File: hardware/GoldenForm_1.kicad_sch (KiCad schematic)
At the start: 56 parts, among them IC1 UVLO, J1 1140084168, J2 Conn_01x02_Pin, J3 USB4105-GF-A, J4 Conn_01x04_Pin, J5 Conn_01x02_Pin, M1 MountingHole x 4, U1 ESP32-S3-WROOM-1, U2 BNO055, U3 Buck_Boost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

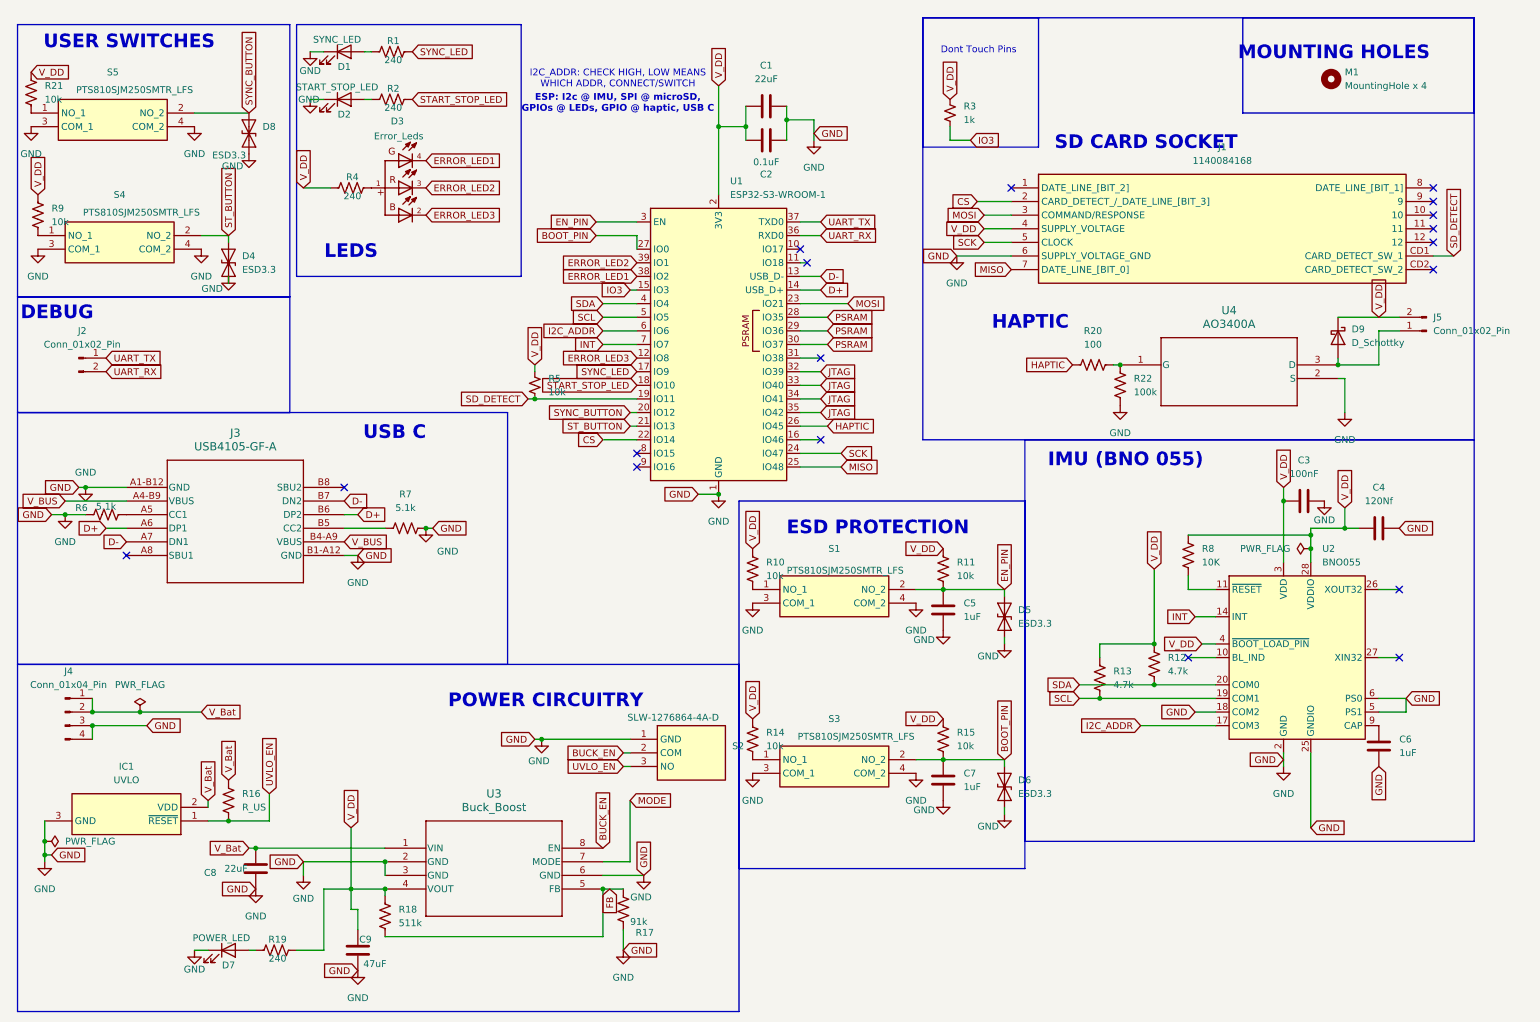
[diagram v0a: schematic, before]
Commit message: added caps for vdd sd, added esd for usbc, fixed i2c addr from bno
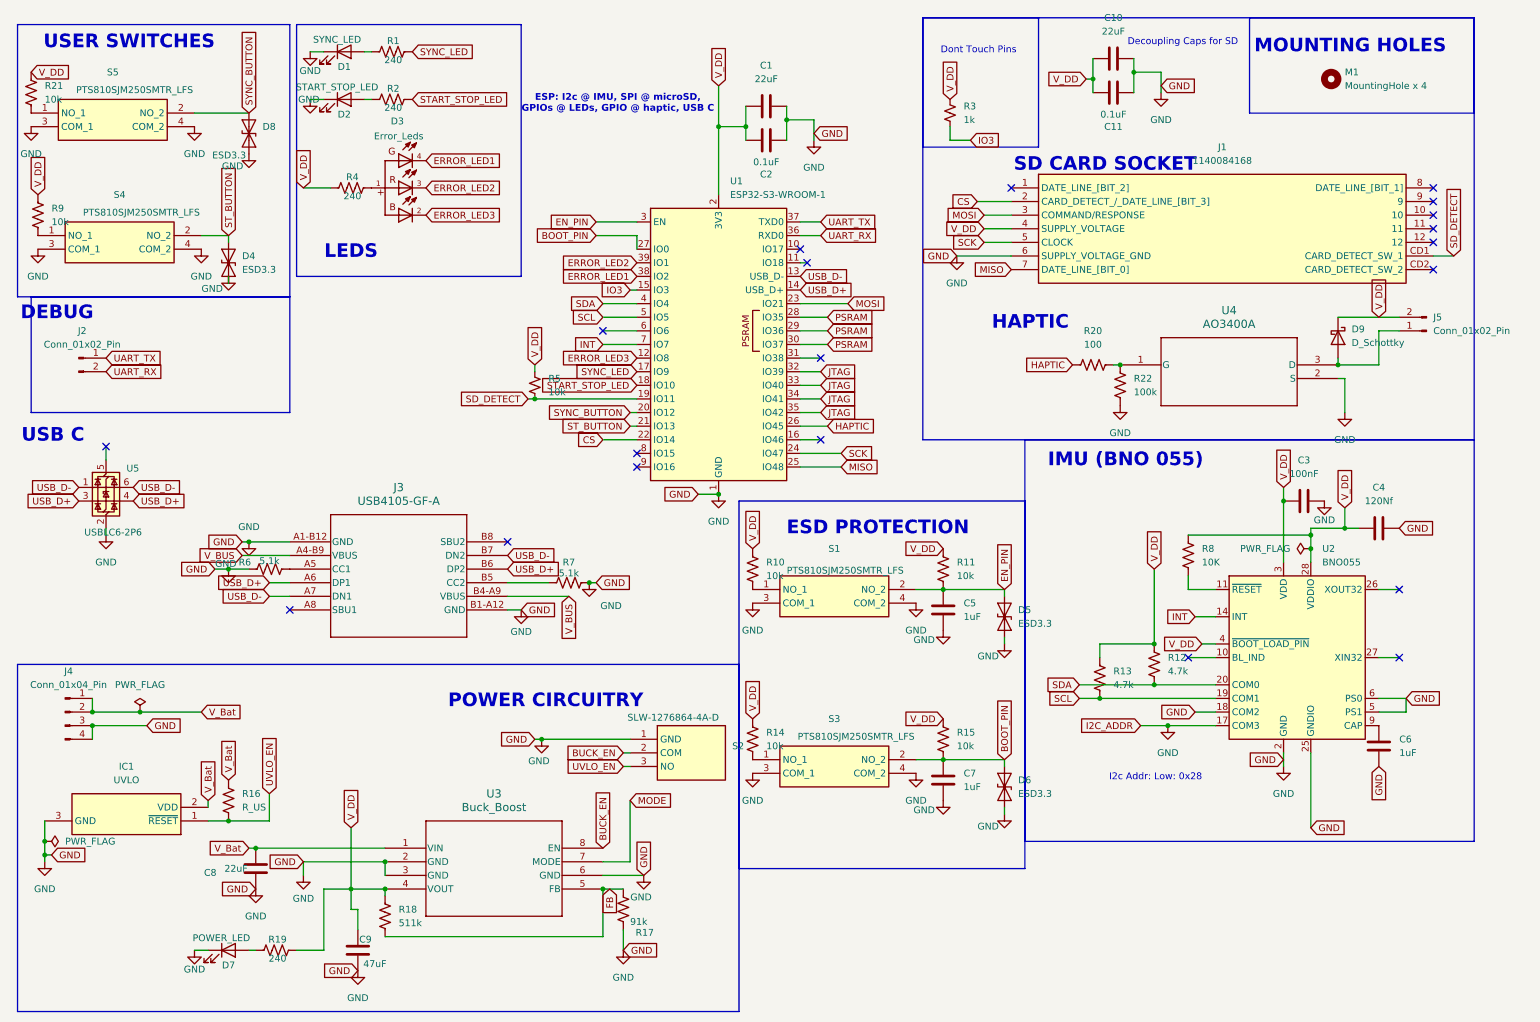
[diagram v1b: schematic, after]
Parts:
- added C10: 22uF, Capacitor_SMD:C_0805_2012Metric_Pad1.18x1.45mm_HandSolder, symbol Device:C
- added C11: 0.1uF, Capacitor_SMD:C_0805_2012Metric_Pad1.18x1.45mm_HandSolder, symbol Device:C
- added U5: USBLC6-2P6, Package_TO_SOT_SMD:SOT-666, symbol Power_Protection:USBLC6-2P6
- D4, D5, D6, D8: footprint Diode_SMD:D_SOD-923 -> Diode_SMD:D_0805_2012Metric_Pad1.15x1.40mm_HandSolder
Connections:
- net GND: now also U2.17 (COM3), C10.2, C11.2, U5.2 (GND)
- net V_DD: now also C10.1, C11.1
- net D+ renamed USB_D+
- net USB_D+: now also U5.3 (I/O2), U5.4 (I/O2)
- net D- renamed USB_D-
- net USB_D-: now also U5.1 (I/O1), U5.6 (I/O1)
- net I2C_ADDR: no longer names the net of U1.6 (IO6)
- net I2C_ADDR: no longer U2.17 (COM3)
- no-connect marks 18 -> 20
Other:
- note added: "Decoupling Caps for SD"
- note added: "I2c Addr: Low: 0x28"
- note removed: "I2C_ADDR: CHECK HIGH, LOW MEANS WHICH ADDR, CONNECT/SWITCH"
- moved on the sheet: J3, R6, R7

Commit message: 0 DRC errors. Need to do silkscreen
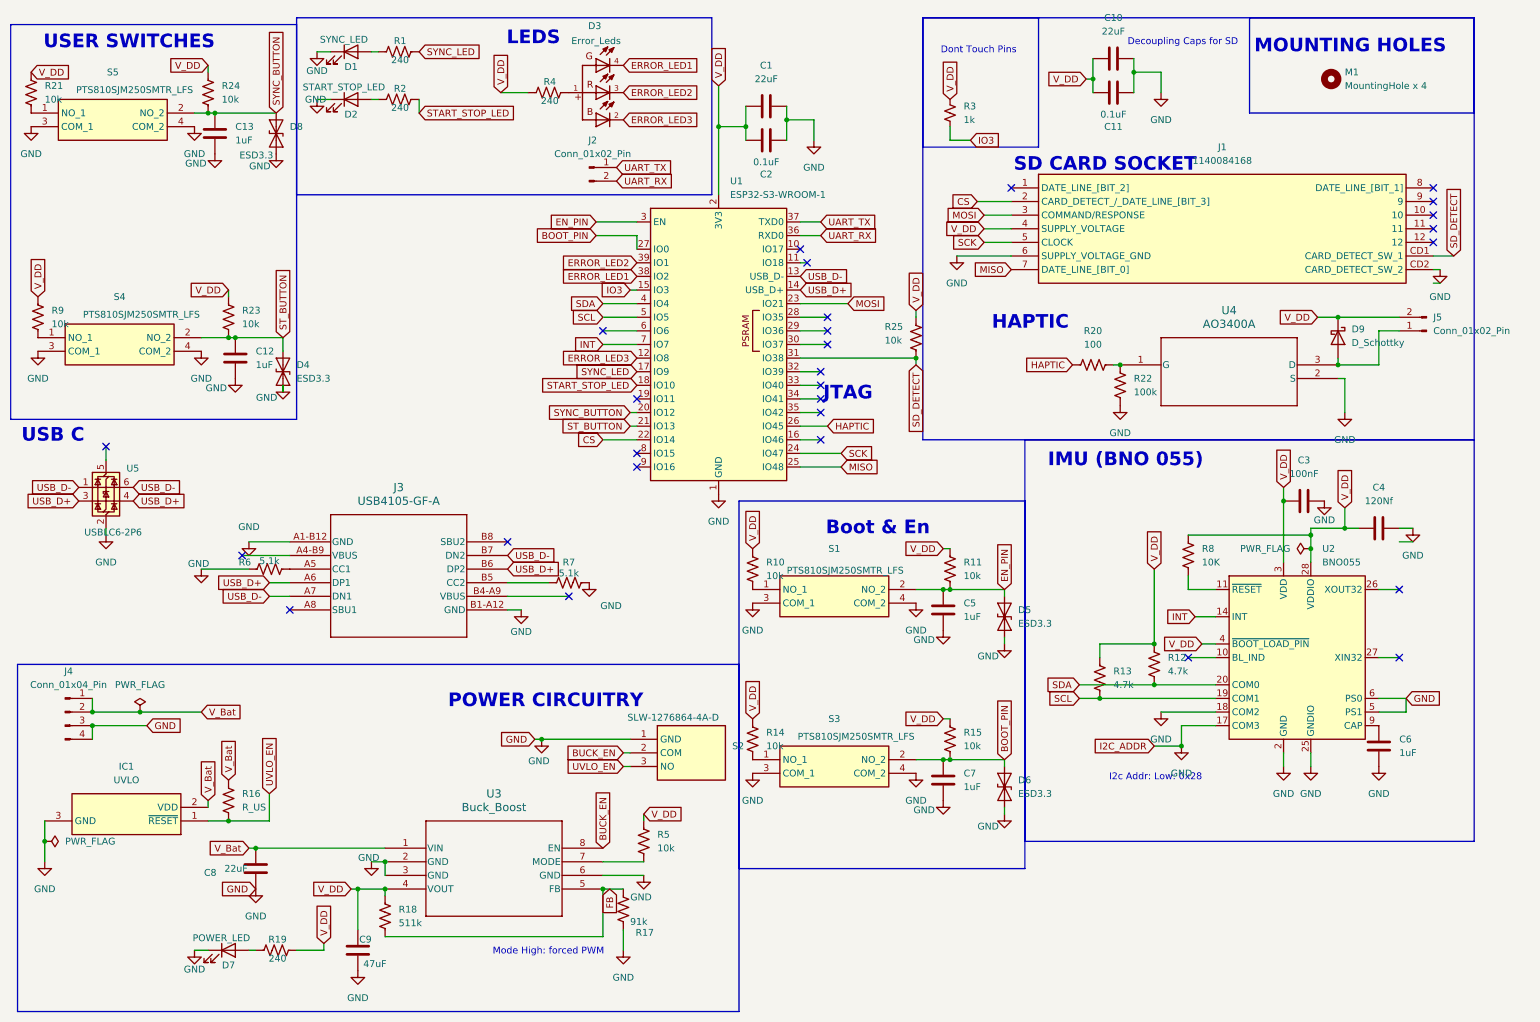
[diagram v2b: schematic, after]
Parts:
- removed R5: 10k, Resistor_SMD:R_0805_2012Metric_Pad1.20x1.40mm_HandSolder, symbol Device:R_Small_US
- added C12, C13: 1uF, Capacitor_SMD:C_0805_2012Metric_Pad1.18x1.45mm_HandSolder, symbol Device:C
- added R23, R24, R25, R5: 10k, Resistor_SMD:R_0805_2012Metric_Pad1.20x1.40mm_HandSolder, symbol Device:R_US
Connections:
- net GND: now also J1.CD2 (CARD_DETECT_SW_2), C12.2, C13.2
- net SD_DETECT: now also U1.31 (IO38), R25.2; no longer U1.19 (IO11)
- net ST_BUTTON: now also C12.1, R23.2
- net SYNC_BUTTON: now also C13.1, R24.2
- net V_DD: now also R23.1, R24.1, R25.1, R5.1
- removed net JTAG: U1.32 (IO39), U1.33 (IO40), U1.34 (IO41), U1.35 (IO42)
- net MODE: no longer names the net of U3.7 (MODE)
- net MODE: now also R5.2
- removed net PSRAM: U1.28 (IO35), U1.29 (IO36), U1.30 (IO37)
- net V_BUS: no longer names the net of J3.A4-B9 (VBUS)
- net V_BUS: no longer J3.B4-A9 (VBUS)
- no-connect marks 20 -> 28
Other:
- note added: "Boot & En"
- note added: "JTAG"
- note added: "Mode High: forced PWM"
- note removed: "DEBUG"
- note removed: "ESD PROTECTION"
- note removed: "ESP: I2c @ IMU, SPI @ microSD, GPIOs @ LEDs, GPIO @ haptic, USB C"
- moved on the sheet: D1, D2, D3, D4, D8, J2, R1, R11, R15, R2, R4, R9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

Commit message: CDR updates
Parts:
- J2: footprint Connector_PinHeader_1.00mm:PinHeader_1x02_P1.00mm_Vertical -> Connector_PinHeader_2.54mm:PinHeader_1x02_P2.54mm_Vertical
- J3: footprint USB4105_GCT -> MyFootprints:USB4105_GCT
- J4: footprint Connector_PinHeader_1.00mm:PinHeader_1x04_P1.00mm_Vertical -> Connector_PinHeader_2.54mm:PinHeader_1x04_P2.54mm_Vertical
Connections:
- net V_BUS: now reaches J3.B4-A9 (VBUS)
- net V_BUS: now also U5.5 (VBUS)
- no-connect marks 28 -> 26
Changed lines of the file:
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@@
 	)
 	(no_connect
-		(at 115.57 119.38)
-	)
-	(no_connect
 		(at 270.51 130.81)
 	)
@@
 	)
 	(no_connect
-		(at 54.61 111.76)
-	)
-	(no_connect
 		(at 163.83 69.85)
 	)
@@
 	)
 	(no_connect
-		(at 29.21 91.44)
-	)
-	(no_connect
 		(at 163.83 67.31)
 	)
@@
 	)
 	(no_connect
+		(at 54.61 111.76)
+	)
+	(no_connect
 		(at 63.5 121.92)
 	)
@@
 	(wire
 		(pts
+			(xy 104.14 119.38) (xy 106.68 119.38)
+		)
+		(stroke
+			(width 0)
+			(type default)
+		)
+	)
+	(wire
+		(pts
 			(xy 45.72 29.21) (xy 48.26 29.21)
 		)
@@
 	(wire
 		(pts
-			(xy 104.14 119.38) (xy 115.57 119.38)
-		)
-		(stroke
-			(width 0)
-			(type default)
-		)
-	)
-	(wire
-		(pts
 			(xy 180.34 149.86) (xy 185.42 149.86)
 		)
@@
 	(wire
 		(pts
+			(xy 29.21 91.44) (xy 31.75 91.44)
+		)
+		(stroke
+			(width 0)
+			(type default)
+		)
+	)
+	(wire
+		(pts
 			(xy 158.75 52.07) (xy 162.56 52.07)
 		)
@@
 		)
 	)
+	(global_label "V_BUS"
+		(shape input)
+		(at 31.75 91.44 0)
+		(fields_autoplaced yes)
+		(effects
+			(font
+				(size 1.27 1.27)
+			)
+			(justify left)
+		)
+		(property "Intersheetrefs" "${INTERSHEET_REFS}"
+			(at 40.6014 91.44 0)
+			(effects
+				(font
+					(size 1.27 1.27)
+				)
+				(justify left)
+				(hide yes)
+			)
+		)
+	)
 	(global_label "HAPTIC"
 		(shape input)
@@
 		)
 	)
+	(global_label "V_BUS"
+		(shape input)
+		(at 106.68 119.38 0)
+		(fields_autoplaced yes)
+		(effects
+			(font
+				(size 1.27 1.27)
+			)
+			(justify left)
+		)
+		(property "Intersheetrefs" "${INTERSHEET_REFS}"
+			(at 115.5314 119.38 0)
+			(effects
+				(font
+					(size 1.27 1.27)
+				)
+				(justify left)
+				(hide yes)
+			)
+		)
+	)
 	(global_label "GND"
 		(shape input)
@@
 			)
 		)
-		(property "Footprint" "Connector_PinHeader_1.00mm:PinHeader_1x04_P1.00mm_Vertical"
+		(property "Footprint" "Connector_PinHeader_2.54mm:PinHeader_1x04_P2.54mm_Vertical"
 			(at 21.59 140.97 0)
 			(effects
@@
 			)
 		)
-		(property "Footprint" "USB4105_GCT"
+		(property "Footprint" "MyFootprints:USB4105_GCT"
 			(at 63.5 109.22 0)
 			(effects
@@
 			)
 		)
-		(property "Footprint" "Connector_PinHeader_1.00mm:PinHeader_1x02_P1.00mm_Vertical"
+		(property "Footprint" "Connector_PinHeader_2.54mm:PinHeader_1x02_P2.54mm_Vertical"
 			(at 119.38 39.37 0)
 			(effects
@@
 		)
 		(property "Value" "GND"
-			(at 46.482 113.284 0)
+			(at 44.196 114.554 0)
 			(effects
 				(font

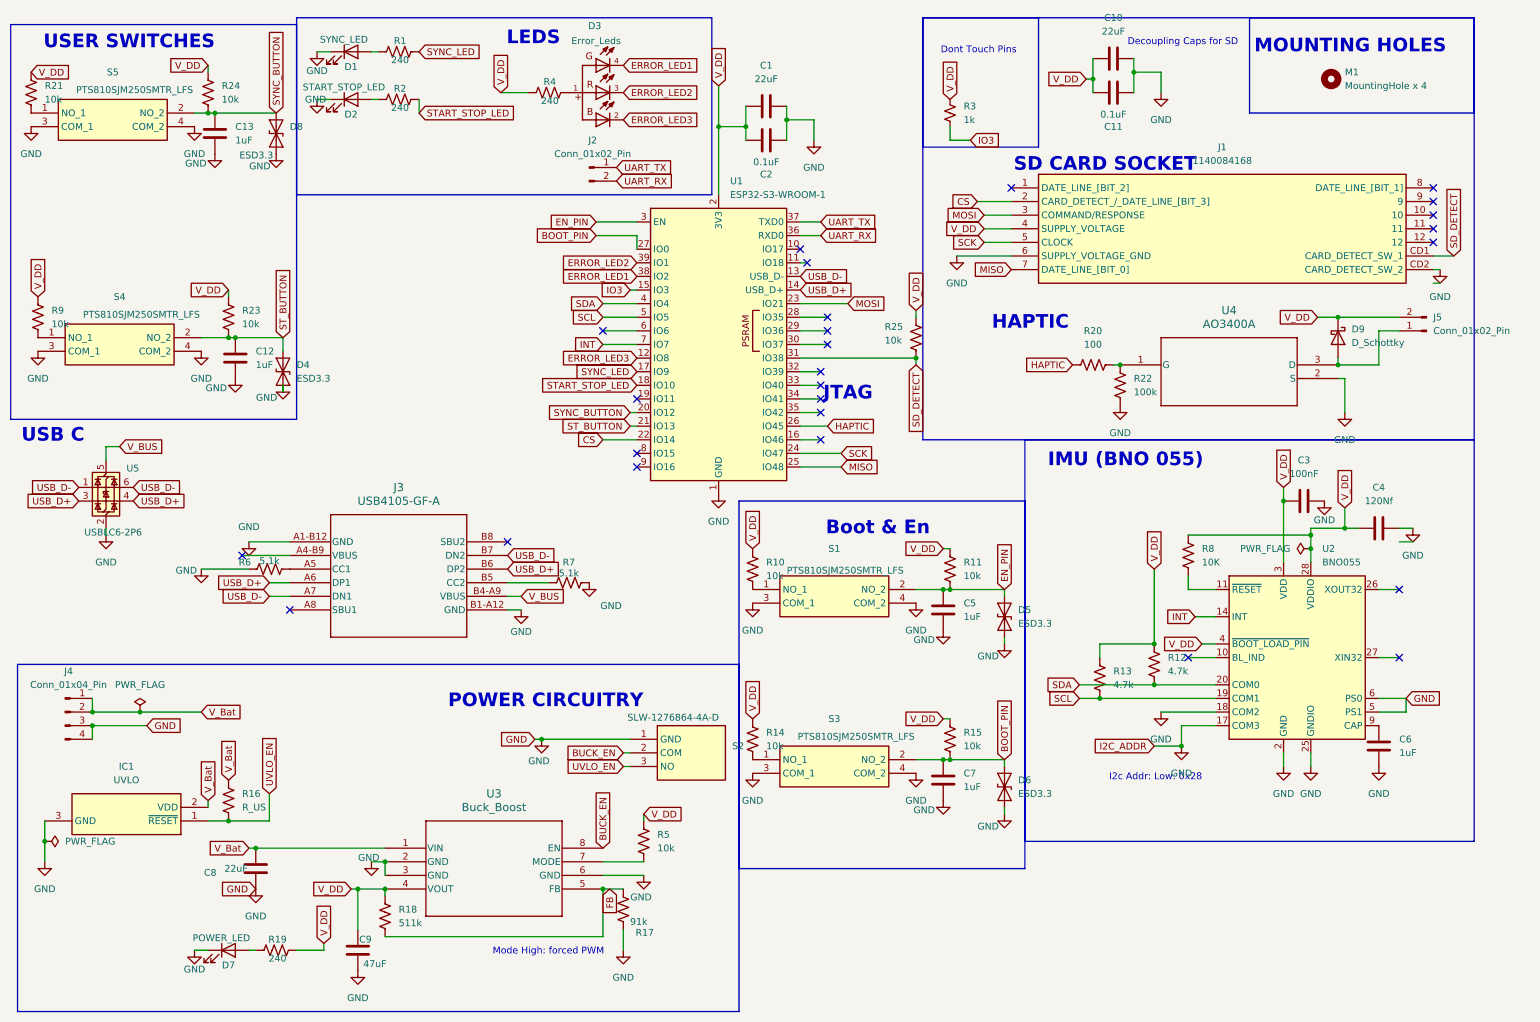
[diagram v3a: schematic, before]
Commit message: added shield res, and ext button headers
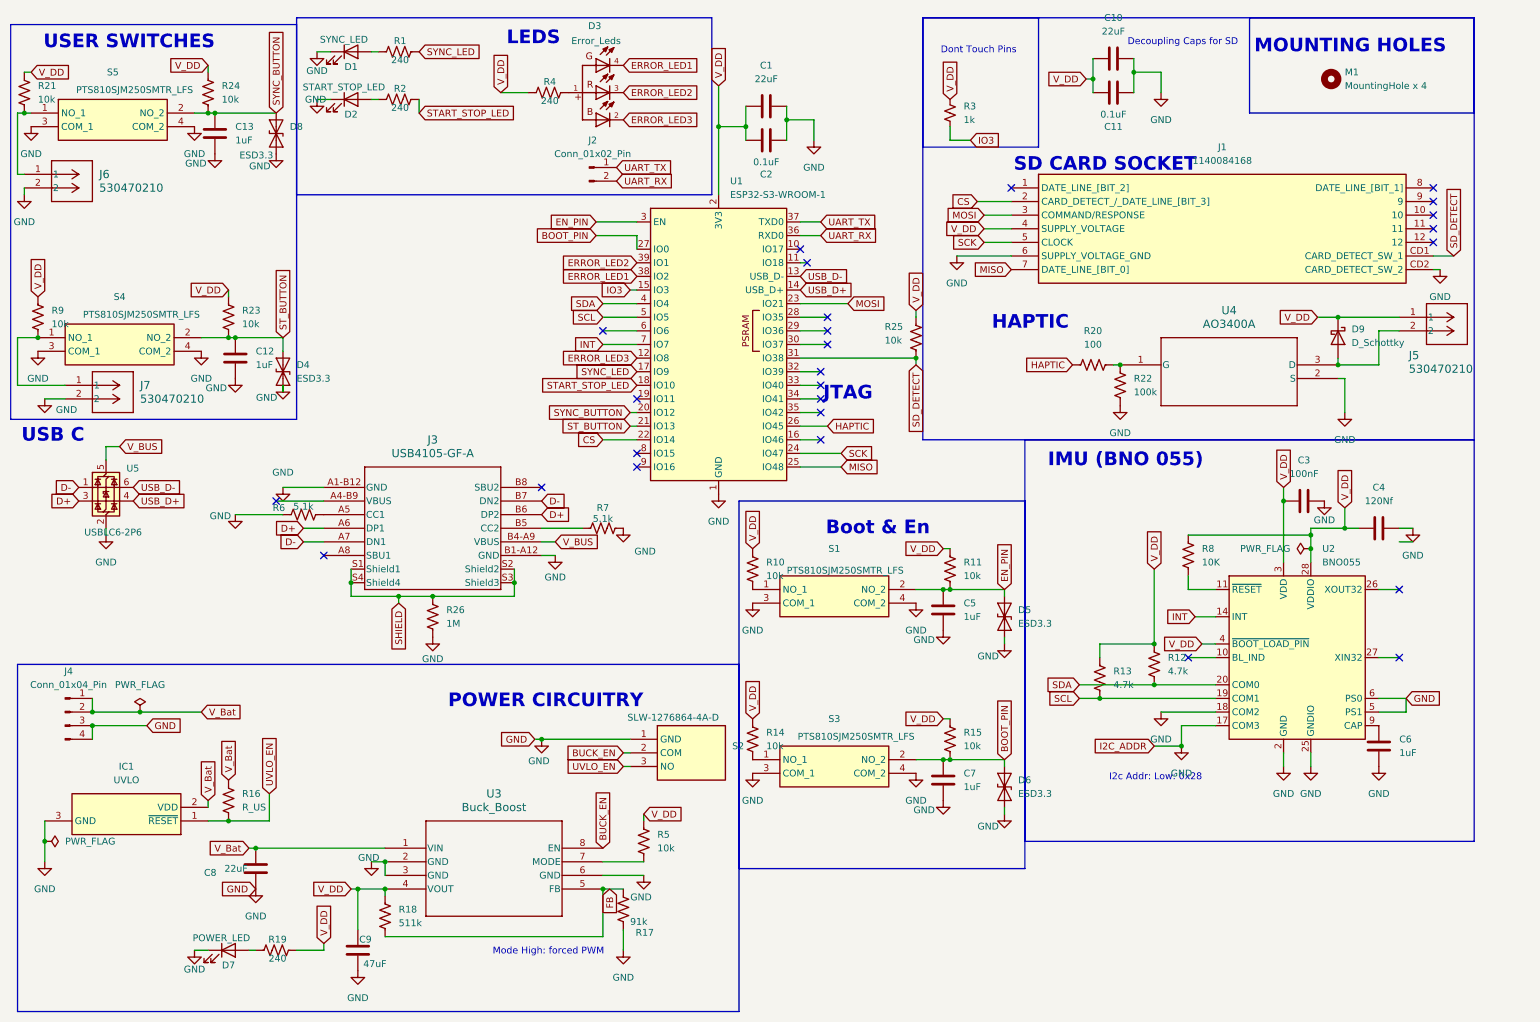
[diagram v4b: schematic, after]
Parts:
- removed J5: Conn_01x02_Pin, Connector_PinHeader_1.00mm:PinHeader_1x02_P1.00mm_Vertical, symbol Connector:Conn_01x02_Pin
- added J5, J6, J7: 530470210, MyFootprints:CONN02_530470210_MOL, symbol MySymbols:530470210
- added R26: 1M, Resistor_SMD:R_0805_2012Metric_Pad1.20x1.40mm_HandSolder, symbol Device:R_US
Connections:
- net GND: now also J6.2, J7.2, R26.2
- net USB_D+: no longer J3.A6 (DP1), J3.B6 (DP2), U5.3 (I/O2)
- net USB_D-: no longer J3.A7 (DN1), J3.B7 (DN2), U5.1 (I/O1)
- net V_DD: now also J5.1
- net at R21.2, S5.1 (NO_1): now also J6.1
- net at D9.2 (A), U4.3 (D): now also J5.2
- net at R9.2, S4.1 (NO_1): now also J7.1
- new net D+: J3.A6 (DP1), J3.B6 (DP2), U5.3 (I/O2)
- new net D-: J3.A7 (DN1), J3.B7 (DN2), U5.1 (I/O1)
- new net SHIELD: J3.S1 (Shield1), J3.S2 (Shield2), J3.S3 (Shield3), J3.S4 (Shield4), R26.1
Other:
- moved on the sheet: R21, R6, R7

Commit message: final PCB
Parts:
- removed R10, R14, R21, R9: 10k, Resistor_SMD:R_0805_2012Metric_Pad1.20x1.40mm_HandSolder, symbol Device:R_US
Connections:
- net HAPTIC: now also U1.11 (IO18); no longer U1.26 (IO45)
- net IO17: now reaches U1.10 (IO17)
- net IO15: now reaches U1.8 (IO15)
- net IO16: now reaches U1.9 (IO16)
- no-connect marks 26 -> 25
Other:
- note added: "IO15,16,17 used for redundancy"
- note added: "IO3, IO45,IO46 + PSRAM"
- note added: "NO 45,46"
